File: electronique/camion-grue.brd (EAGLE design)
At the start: 160 x 100 mm, 52 parts

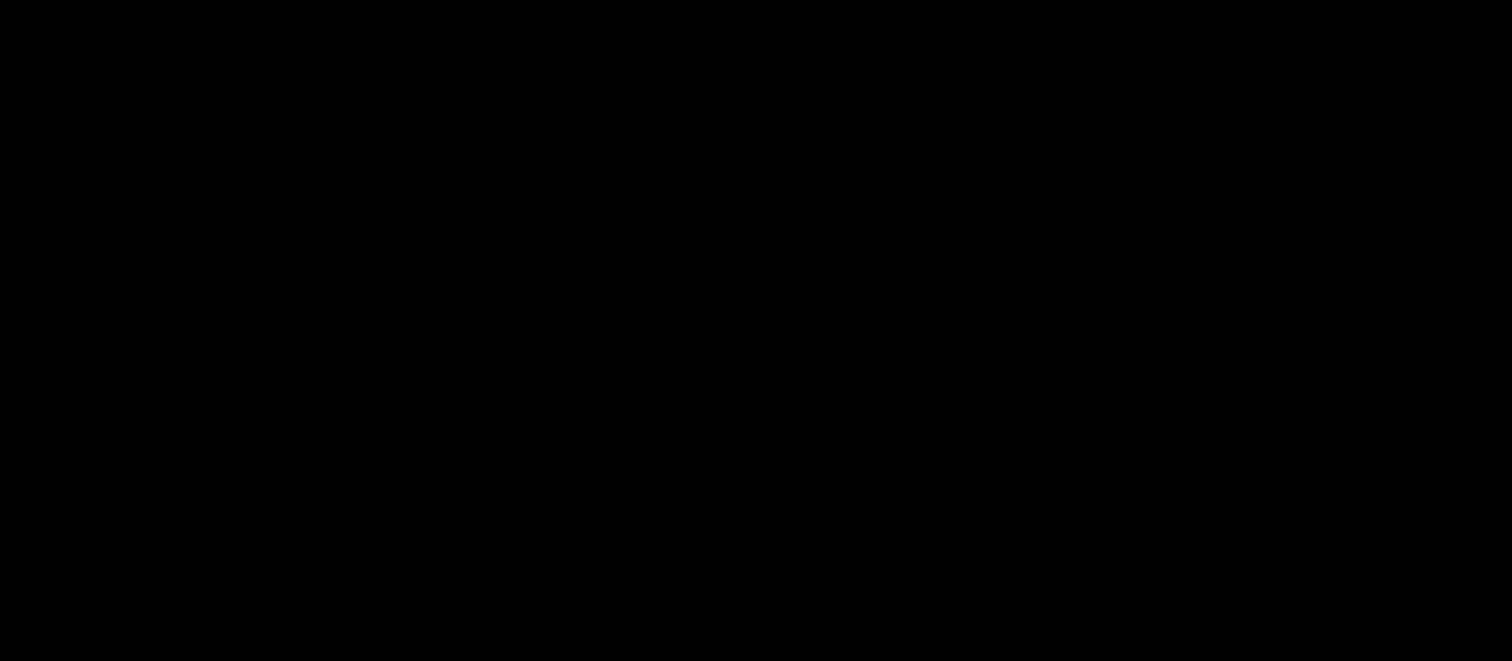
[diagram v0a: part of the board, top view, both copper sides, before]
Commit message: Ajout libs Eagle
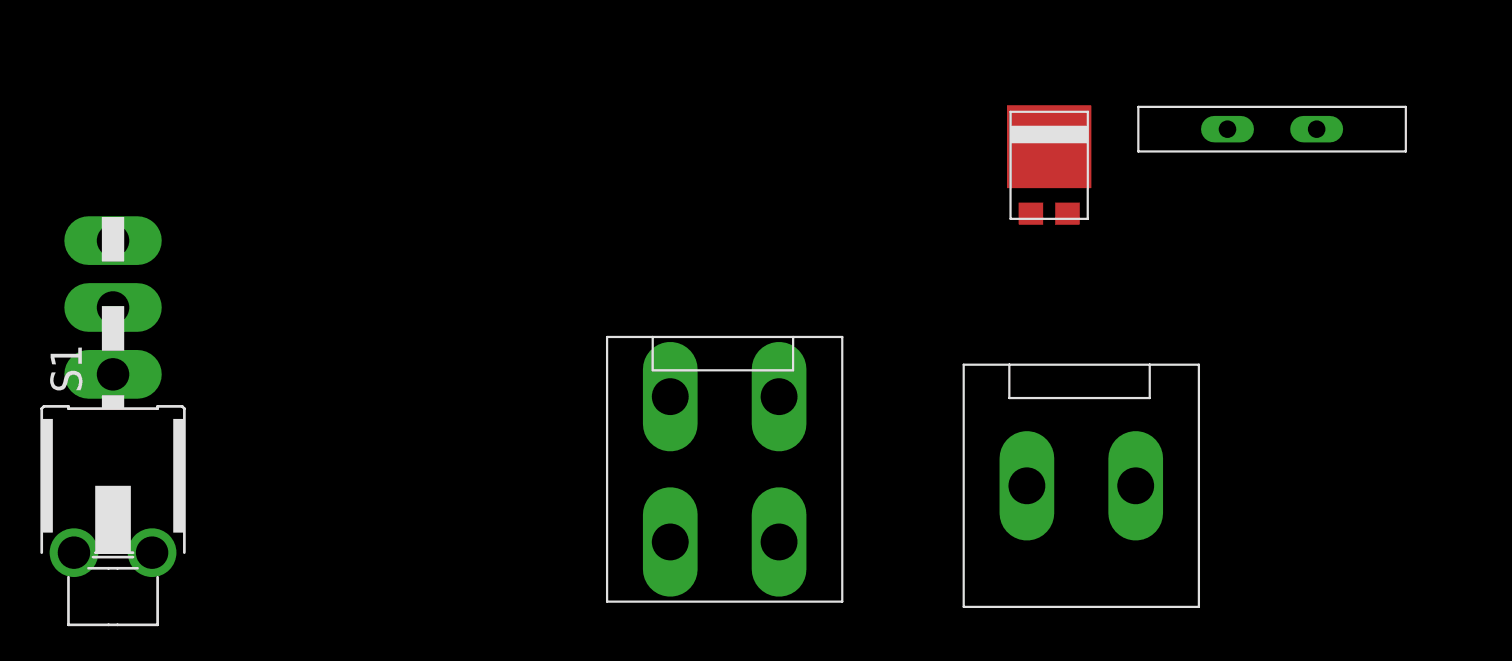
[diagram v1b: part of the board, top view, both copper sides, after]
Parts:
- added ALIM-GRUE: JST-02VL-V, con-jst:VL-02-V
- added D1: DIODE_S15P45, diode_schottky:TO-277A
- added LIPO-ET-ARRET-URGENCE: JST-04VL-V, con-jst:VL-04-V
- added P1: RGEF800, polyswitch:5MM
- added S1: (no value), switch:SWITCH_LPV-1
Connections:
- new net N$2: LIPO-ET-ARRET-URGENCE.1, P1.P$2
- new net N$3: D1.-, LIPO-ET-ARRET-URGENCE.3, S1.2
- new net N$4: D1.+1, D1.+2, P1.P$1
- net +12V: now also ALIM-GRUE.1, LIPO-ET-ARRET-URGENCE.4
- net 12V_AUX: now also S1.3
- net GND: now also ALIM-GRUE.2, LIPO-ET-ARRET-URGENCE.2
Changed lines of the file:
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@@
 <element name="LED1" library="led" library_urn="urn:adsk.eagle:library:259" package="1206" package3d_urn="urn:adsk.eagle:package:15796/1" value="" x="-106.68" y="-448.31"/>
 <element name="R1" library="resistor" library_urn="urn:adsk.eagle:library:348" package="R0805" package3d_urn="urn:adsk.eagle:package:26059/1" value="" x="-107.95" y="-454.66"/>
+<element name="D1" library="diode_schottky" package="TO-277A" value="DIODE_S15P45" x="-111.76" y="-541.02"/>
+<element name="P1" library="polyswitch" package="5MM" value="RGEF800" x="-99.06" y="-537.21">
+<attribute name="RS" value="517-6966" x="-99.06" y="-537.21" size="1.778" layer="27" display="off"/>
+</element>
+<element name="ALIM-GRUE" library="con-jst" package="VL-02-V" value="JST-02VL-V" x="-113.03" y="-557.53"/>
+<element name="LIPO-ET-ARRET-URGENCE" library="con-jst" package="VL-04-V" value="JST-04VL-V" x="-133.35" y="-552.45"/>
+<element name="S1" library="switch" package="SWITCH_LPV-1" value="" x="-165.1" y="-561.34">
+<attribute name="RS" value="734-7306" x="-165.1" y="-561.34" size="1.778" layer="27" display="off"/>
+</element>
 </elements>
 <signals>
@@
 <contactref element="DC4" pad="2"/>
 <contactref element="LED1" pad="C"/>
+<contactref element="ALIM-GRUE" pad="2"/>
+<contactref element="LIPO-ET-ARRET-URGENCE" pad="2"/>
 <wire x1="-64.45" y1="-198.12" x2="-61.28" y2="-191.77" width="0" layer="19" extent="1-1"/>
 <wire x1="-60.96" y1="-179.07" x2="-61.28" y2="-191.77" width="0" layer="19" extent="1-1"/>
@@
 <wire x1="-11.43" y1="26.67" x2="-52.07" y2="-17.78" width="0" layer="19" extent="1-1"/>
 <wire x1="-26.67" y1="62.23" x2="-11.43" y2="26.67" width="0" layer="19" extent="1-1"/>
+<wire x1="-127.15" y1="-552.45" x2="-105.258" y2="-448.31" width="0" layer="19" extent="1-1"/>
+<wire x1="-106.83" y1="-557.53" x2="-127.15" y2="-552.45" width="0" layer="19" extent="1-1"/>
 </signal>
 <signal name="VIN">
@@
 <contactref element="DC4" pad="1"/>
 <contactref element="C4" pad="+"/>
+<contactref element="ALIM-GRUE" pad="1"/>
+<contactref element="LIPO-ET-ARRET-URGENCE" pad="4"/>
 <wire x1="-101.6" y1="-387.35" x2="-101.6" y2="-403.86" width="0" layer="19" extent="1-1"/>
 <wire x1="-101.6" y1="-370.84" x2="-101.6" y2="-387.35" width="0" layer="19" extent="1-1"/>
@@
 <wire x1="-76.52" y1="-30.48" x2="-71.12" y2="-71.12" width="0" layer="19" extent="1-1"/>
 <wire x1="-66.04" y1="-12.7" x2="-76.52" y2="-30.48" width="0" layer="19" extent="1-1"/>
+<wire x1="-113.03" y1="-557.53" x2="-101.6" y2="-436.88" width="0" layer="19" extent="1-1"/>
+<wire x1="-127.15" y1="-560.73" x2="-113.03" y2="-557.53" width="0" layer="19" extent="1-1"/>
 </signal>
 <signal name="MOT_AV_G_EN">
@@
 <contactref element="C3" pad="+"/>
 <contactref element="DC3" pad="1"/>
+<contactref element="S1" pad="3"/>
 <wire x1="-101.6" y1="-420.37" x2="-101.6" y2="-353.06" width="0" layer="19" extent="1-1"/>
+<wire x1="-165.1" y1="-543.56" x2="-101.6" y2="-420.37" width="0" layer="19" extent="1-1"/>
 </signal>
 <signal name="+6V5">
@@
 <wire x1="-108.102" y1="-448.31" x2="-108.9" y2="-454.66" width="0" layer="19" extent="1-1"/>
 </signal>
+<signal name="N$3">
+<contactref element="D1" pad="-"/>
+<contactref element="LIPO-ET-ARRET-URGENCE" pad="3"/>
+<contactref element="S1" pad="2"/>
+<wire x1="-133.35" y1="-560.73" x2="-165.1" y2="-547.37" width="0" layer="19" extent="1-1"/>
+<wire x1="-111.76" y1="-538.21" x2="-133.35" y2="-560.73" width="0" layer="19" extent="1-1"/>
+</signal>
+<signal name="N$2">
+<contactref element="P1" pad="P$2"/>
+<contactref element="LIPO-ET-ARRET-URGENCE" pad="1"/>
+<wire x1="-96.52" y1="-537.21" x2="-133.35" y2="-552.45" width="0" layer="19" extent="1-1"/>
+</signal>
+<signal name="N$4">
+<contactref element="P1" pad="P$1"/>
+<contactref element="D1" pad="+1"/>
+<contactref element="D1" pad="+2"/>
+<wire x1="-112.8" y1="-542.02" x2="-101.6" y2="-537.21" width="0" layer="19" extent="1-1"/>
+<wire x1="-110.72" y1="-542.02" x2="-112.8" y2="-542.02" width="0" layer="19" extent="1-1"/>
+</signal>
 </signals>

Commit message: maj elec et libs eagle
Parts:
- added ENCODEUR_DROIT, ENCODEUR_GAUCHE: JST-04GH-V, con-jst:GH-04-V
- added FEUX_ARRIERE: JST-06, con-jst:GH-06-V
- added LED2, LED3: (no value), led:1206
- added MOT_AR_D, MOT_AR_G, MOT_AV_D, MOT_AV_G: (no value), pinhead:1X06
- added Q1, Q2: BSS138, transistor-small-signal:SOT23
- added R2, R3, R6, R7: 10k, resistor:R0805
- added R4, R5: 330, resistor:R0805
- added S3: TL36PO, switch:TL3XPO
- added SERIAL_GRUE: JST-02GH-V, con-jst:GH-02-V
- added TOF_FLAN_AV_D, TOF_FLAN_AV_G: JST-05, con-jst:GH-05-V
- R1: value (none) -> 470
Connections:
- new net CHOOSE_COLOR: LED3.C, R4.2, S3.2
- new net N$7: LED2.A, R4.1
- new net N$8: LED3.A, R5.2
- new net SERIAL_AX12: Q1.2, R2.2
- new net SERIAL_AX12_5V: Q1.3, R3.2
- new net SERIAL_XL320: Q2.2, R6.2
- new net SERIAL_XL320_5V: Q2.3, R7.2
- net +3V3: now also Q1.1, Q2.1, R2.1, R5.1, R6.1, S3.3
- net +5V: now also R3.1, R7.1
- net GND: now also LED2.C, S3.1
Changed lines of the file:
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@@
 <element name="C4" library="resistor" library_urn="urn:adsk.eagle:library:348" package="E2,5-7" package3d_urn="urn:adsk.eagle:package:25830/1" value="" x="-100.33" y="-436.88"/>
 <element name="LED1" library="led" library_urn="urn:adsk.eagle:library:259" package="1206" package3d_urn="urn:adsk.eagle:package:15796/1" value="" x="-106.68" y="-448.31"/>
-<element name="R1" library="resistor" library_urn="urn:adsk.eagle:library:348" package="R0805" package3d_urn="urn:adsk.eagle:package:26059/1" value="" x="-107.95" y="-454.66"/>
+<element name="R1" library="resistor" library_urn="urn:adsk.eagle:library:348" package="R0805" package3d_urn="urn:adsk.eagle:package:26059/1" value="470" x="-107.95" y="-454.66"/>
 <element name="D1" library="diode_schottky" package="TO-277A" value="DIODE_S15P45" x="-111.76" y="-541.02"/>
 <element name="P1" library="polyswitch" package="5MM" value="RGEF800" x="-99.06" y="-537.21">
@@
 <attribute name="RS" value="734-7306" x="-165.1" y="-561.34" size="1.778" layer="27" display="off"/>
 </element>
+<element name="Q1" library="transistor-small-signal" library_urn="urn:adsk.eagle:library:401" package="SOT23" package3d_urn="urn:adsk.eagle:package:29752/1" value="BSS138" x="-177.8" y="-580.39"/>
+<element name="R2" library="resistor" library_urn="urn:adsk.eagle:library:348" package="R0805" package3d_urn="urn:adsk.eagle:package:26059/1" value="10k" x="-179.07" y="-588.01"/>
+<element name="R3" library="resistor" library_urn="urn:adsk.eagle:library:348" package="R0805" package3d_urn="urn:adsk.eagle:package:26059/1" value="10k" x="-179.07" y="-594.36"/>
+<element name="S3" library="switch" library_urn="urn:adsk.eagle:library:380" package="TL3XPO" package3d_urn="urn:adsk.eagle:package:27745/1" value="TL36PO" x="-170.18" y="-623.57"/>
+<element name="LED2" library="led" library_urn="urn:adsk.eagle:library:259" package="1206" package3d_urn="urn:adsk.eagle:package:15796/1" value="" x="-177.8" y="-635"/>
+<element name="LED3" library="led" library_urn="urn:adsk.eagle:library:259" package="1206" package3d_urn="urn:adsk.eagle:package:15796/1" value="" x="-177.8" y="-641.35"/>
+<element name="R4" library="resistor" library_urn="urn:adsk.eagle:library:348" package="R0805" package3d_urn="urn:adsk.eagle:package:26059/1" value="330" x="-179.07" y="-647.7"/>
+<element name="R5" library="resistor" library_urn="urn:adsk.eagle:library:348" package="R0805" package3d_urn="urn:adsk.eagle:package:26059/1" value="330" x="-179.07" y="-654.05"/>
+<element name="Q2" library="transistor-small-signal" library_urn="urn:adsk.eagle:library:401" package="SOT23" package3d_urn="urn:adsk.eagle:package:29752/1" value="BSS138" x="-177.8" y="-661.67"/>
+<element name="R6" library="resistor" library_urn="urn:adsk.eagle:library:348" package="R0805" package3d_urn="urn:adsk.eagle:package:26059/1" value="10k" x="-179.07" y="-669.29"/>
+<element name="R7" library="resistor" library_urn="urn:adsk.eagle:library:348" package="R0805" package3d_urn="urn:adsk.eagle:package:26059/1" value="10k" x="-179.07" y="-675.64"/>
+<element name="ENCODEUR_GAUCHE" library="con-jst" package="GH-04-V" value="JST-04GH-V" x="-186.69" y="-673.1"/>
+<element name="ENCODEUR_DROIT" library="con-jst" package="GH-04-V" value="JST-04GH-V" x="-195.58" y="-673.1"/>
+<element name="MOT_AV_G" library="pinhead" library_urn="urn:adsk.eagle:library:325" package="1X06" package3d_urn="urn:adsk.eagle:package:22472/2" value="" x="-185.42" y="-687.07"/>
+<element name="MOT_AV_D" library="pinhead" library_urn="urn:adsk.eagle:library:325" package="1X06" package3d_urn="urn:adsk.eagle:package:22472/2" value="" x="-185.42" y="-702.31"/>
+<element name="MOT_AR_G" library="pinhead" library_urn="urn:adsk.eagle:library:325" package="1X06" package3d_urn="urn:adsk.eagle:package:22472/2" value="" x="-185.42" y="-717.55"/>
+<element name="MOT_AR_D" library="pinhead" library_urn="urn:adsk.eagle:library:325" package="1X06" package3d_urn="urn:adsk.eagle:package:22472/2" value="" x="-185.42" y="-732.79"/>
+<element name="SERIAL_GRUE" library="con-jst" package="GH-02-V" value="JST-02GH-V" x="-204.47" y="-734.06"/>
+<element name="TOF_FLAN_AV_G" library="con-jst" package="GH-05-V" value="JST-05" x="-213.36" y="-734.06"/>
+<element name="TOF_FLAN_AV_D" library="con-jst" package="GH-05-V" value="JST-05" x="-223.52" y="-734.06"/>
+<element name="FEUX_ARRIERE" library="con-jst" package="GH-06-V" value="JST-06" x="-222.25" y="-746.76"/>
 </elements>
 <signals>
@@
 <contactref element="ALIM-GRUE" pad="2"/>
 <contactref element="LIPO-ET-ARRET-URGENCE" pad="2"/>
+<contactref element="S3" pad="1"/>
+<contactref element="LED2" pad="C"/>
 <wire x1="-64.45" y1="-198.12" x2="-61.28" y2="-191.77" width="0" layer="19" extent="1-1"/>
 <wire x1="-60.96" y1="-179.07" x2="-61.28" y2="-191.77" width="0" layer="19" extent="1-1"/>
@@
 <wire x1="-127.15" y1="-552.45" x2="-105.258" y2="-448.31" width="0" layer="19" extent="1-1"/>
 <wire x1="-106.83" y1="-557.53" x2="-127.15" y2="-552.45" width="0" layer="19" extent="1-1"/>
+<wire x1="-172.72" y1="-623.57" x2="-127.15" y2="-552.45" width="0" layer="19" extent="1-1"/>
+<wire x1="-176.378" y1="-635" x2="-172.72" y2="-623.57" width="0" layer="19" extent="1-1"/>
 </signal>
 <signal name="VIN">
@@
 <contactref element="DC3" pad="3"/>
 <contactref element="R1" pad="2"/>
+<contactref element="R3" pad="1"/>
+<contactref element="R7" pad="1"/>
 <wire x1="-59.69" y1="-215.9" x2="-22.86" y2="-215.9" width="0" layer="19" extent="1-1"/>
 <wire x1="-62.55" y1="-198.12" x2="-59.69" y2="-215.9" width="0" layer="19" extent="1-1"/>
@@
 <wire x1="-76.52" y1="-36.83" x2="-59.69" y2="-143.51" width="0" layer="19" extent="1-1"/>
 <wire x1="-59.69" y1="-17.78" x2="-76.52" y2="-36.83" width="0" layer="19" extent="1-1"/>
+<wire x1="-180.02" y1="-594.36" x2="-107" y2="-454.66" width="0" layer="19" extent="1-1"/>
+<wire x1="-180.02" y1="-675.64" x2="-180.02" y2="-594.36" width="0" layer="19" extent="1-1"/>
 </signal>
 <signal name="+12V">
@@
 <signal name="+3V3">
 <contactref element="DC1" pad="3"/>
+<contactref element="Q1" pad="1"/>
+<contactref element="R2" pad="1"/>
+<contactref element="S3" pad="3"/>
+<contactref element="R5" pad="1"/>
+<contactref element="R6" pad="1"/>
+<contactref element="Q2" pad="1"/>
+<wire x1="-180.02" y1="-588.01" x2="-178.75" y2="-581.49" width="0" layer="19" extent="1-1"/>
+<wire x1="-167.64" y1="-623.57" x2="-180.02" y2="-588.01" width="0" layer="19" extent="1-1"/>
+<wire x1="-180.02" y1="-654.05" x2="-167.64" y2="-623.57" width="0" layer="19" extent="1-1"/>
+<wire x1="-178.75" y1="-662.77" x2="-180.02" y2="-654.05" width="0" layer="19" extent="1-1"/>
+<wire x1="-180.02" y1="-669.29" x2="-178.75" y2="-662.77" width="0" layer="19" extent="1-1"/>
+<wire x1="-96.52" y1="-317.5" x2="-178.75" y2="-581.49" width="0" layer="19" extent="1-1"/>
 </signal>
 <signal name="+3V3_LEDS">
@@
 <wire x1="-110.72" y1="-542.02" x2="-112.8" y2="-542.02" width="0" layer="19" extent="1-1"/>
 </signal>
+<signal name="SERIAL_AX12">
+<contactref element="R2" pad="2"/>
+<contactref element="Q1" pad="2"/>
+<wire x1="-178.12" y1="-588.01" x2="-176.85" y2="-581.49" width="0" layer="19" extent="1-1"/>
+</signal>
+<signal name="SERIAL_AX12_5V">
+<contactref element="Q1" pad="3"/>
+<contactref element="R3" pad="2"/>
+<wire x1="-178.12" y1="-594.36" x2="-177.8" y2="-579.29" width="0" layer="19" extent="1-1"/>
+</signal>
+<signal name="CHOOSE_COLOR">
+<contactref element="S3" pad="2"/>
+<contactref element="R4" pad="2"/>
+<contactref element="LED3" pad="C"/>
+<wire x1="-176.378" y1="-641.35" x2="-178.12" y2="-647.7" width="0" layer="19" extent="1-1"/>
+<wire x1="-170.18" y1="-623.57" x2="-176.378" y2="-641.35" width="0" layer="19" extent="1-1"/>
+</signal>
+<signal name="N$7">
+<contactref element="LED2" pad="A"/>
+<contactref element="R4" pad="1"/>
+<wire x1="-179.222" y1="-635" x2="-180.02" y2="-647.7" width="0" layer="19" extent="1-1"/>
+</signal>
+<signal name="N$8">
+<contactref element="LED3" pad="A"/>
+<contactref element="R5" pad="2"/>
+<wire x1="-179.222" y1="-641.35" x2="-178.12" y2="-654.05" width="0" layer="19" extent="1-1"/>
+</signal>
+<signal name="SERIAL_XL320_5V">
+<contactref element="Q2" pad="3"/>
+<contactref element="R7" pad="2"/>
+<wire x1="-177.8" y1="-660.57" x2="-178.12" y2="-675.64" width="0" layer="19" extent="1-1"/>
+</signal>
+<signal name="SERIAL_XL320">
+<contactref element="Q2" pad="2"/>
+<contactref element="R6" pad="2"/>
+<wire x1="-176.85" y1="-662.77" x2="-178.12" y2="-669.29" width="0" layer="19" extent="1-1"/>
+</signal>
 </signals>
